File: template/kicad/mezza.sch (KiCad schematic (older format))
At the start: 2 parts, among them P1 CONN_02X20, P2 CONN_02X20

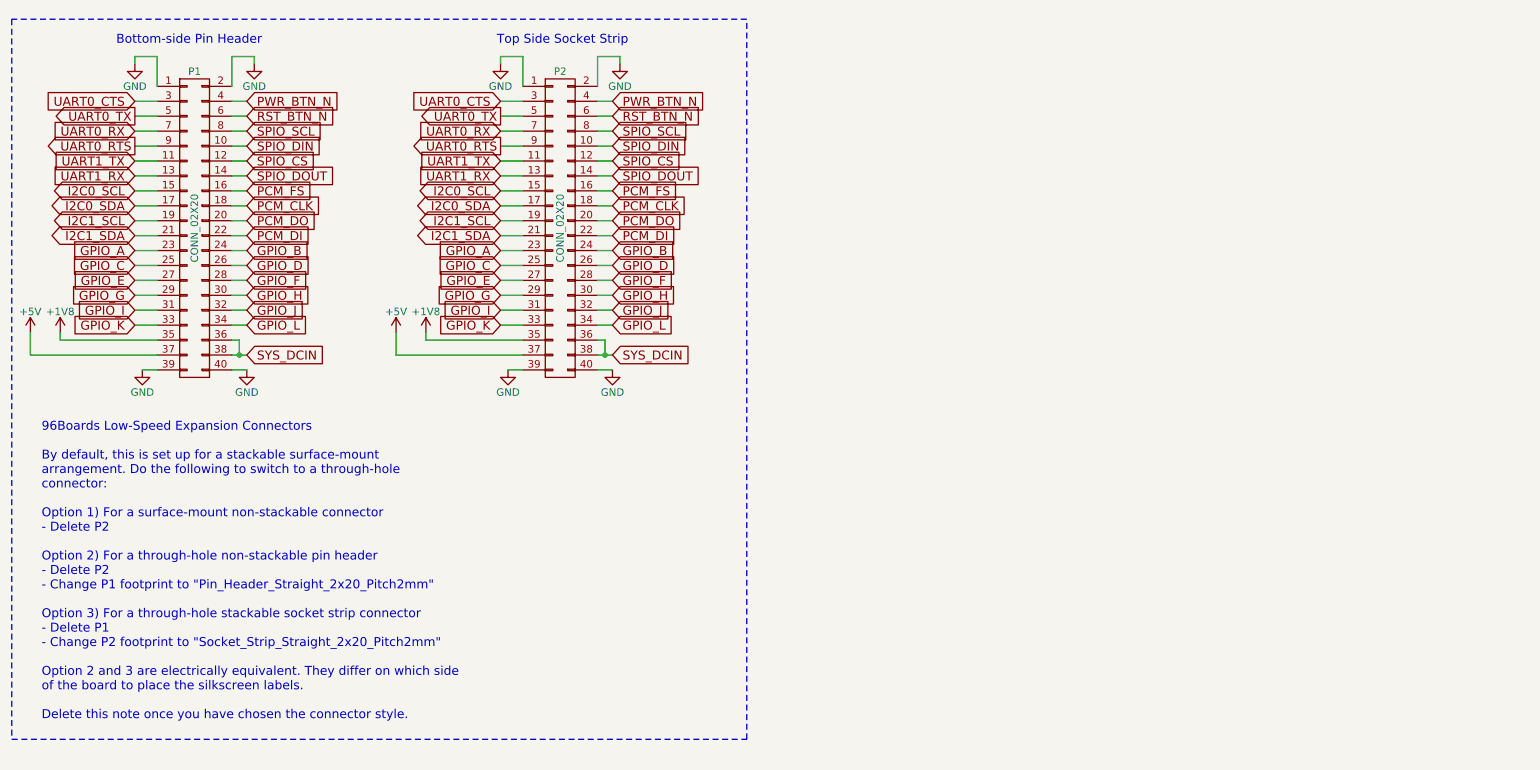
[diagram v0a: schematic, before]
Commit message: Add high speed connector to kicad template
Schematic connector added with net names.
3D model included for PCB footprint.

Signed-off-by: Michael Welling <mwelling@ieee.org>
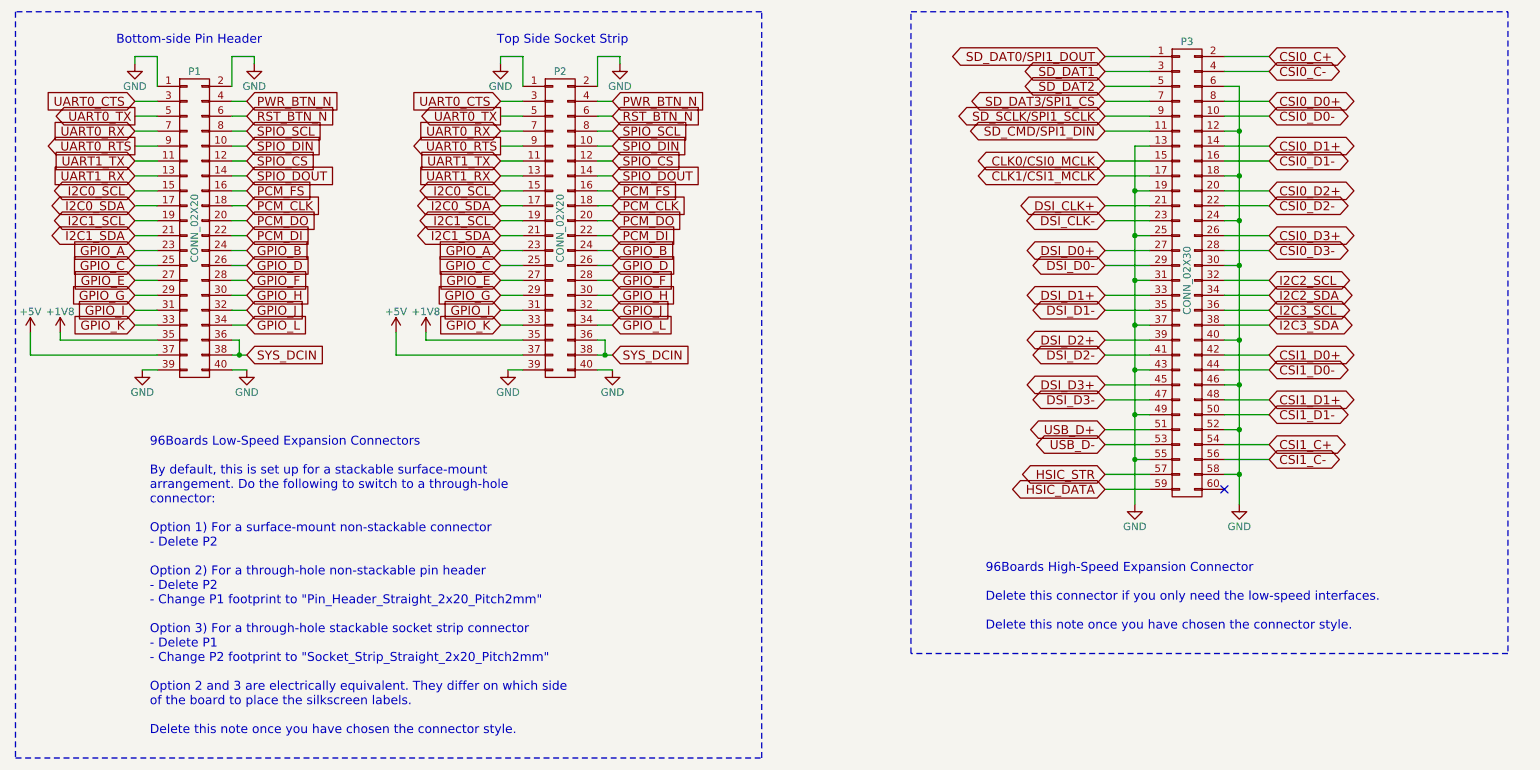
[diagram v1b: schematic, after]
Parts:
- added P3: CONN_02X30, 96boards:61083-063400LF, symbol CONN_02X30
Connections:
- net GND: now also P3.12 (P12), P3.13 (P13), P3.18 (P18), P3.19 (P19), P3.24 (P24), P3.25 (P25), P3.30 (P30), P3.31 (P31), P3.37 (P37), P3.40 (P40), P3.43 (P43), P3.46 (P46), P3.49 (P49), P3.52 (P52), P3.55 (P55), P3.58 (P58), P3.6 (P6)
- new net CLK0/CSI0_MCLK: P3.15 (P15)
- new net CLK1/CSI1_MCLK: P3.17 (P17)
- new net CSI0_C+: P3.2 (P2)
- new net CSI0_C-: P3.4 (P4)
- new net CSI0_D0+: P3.8 (P8)
- new net CSI0_D0-: P3.10 (P10)
- new net CSI0_D1+: P3.14 (P14)
- new net CSI0_D1-: P3.16 (P16)
- new net CSI0_D2+: P3.20 (P20)
- new net CSI0_D2-: P3.22 (P22)
- new net CSI0_D3+: P3.26 (P26)
- new net CSI0_D3-: P3.28 (P28)
- new net CSI1_C+: P3.54 (P54)
- new net CSI1_C-: P3.56 (P56)
- new net CSI1_D0+: P3.42 (P42)
- new net CSI1_D0-: P3.44 (P44)
- new net CSI1_D1+: P3.48 (P48)
- new net CSI1_D1-: P3.50 (P50)
- new net DSI_CLK+: P3.21 (P21)
- new net DSI_CLK-: P3.23 (P23)
- new net DSI_D0+: P3.27 (P27)
- new net DSI_D0-: P3.29 (P29)
- new net DSI_D1+: P3.33 (P33)
- new net DSI_D1-: P3.35 (P35)
- new net DSI_D2+: P3.39 (P39)
- new net DSI_D2-: P3.41 (P41)
- new net DSI_D3+: P3.45 (P45)
- new net DSI_D3-: P3.47 (P47)
- new net HSIC_DATA: P3.59 (P59)
- new net HSIC_STR: P3.57 (P57)
- new net I2C2_SCL: P3.32 (P32)
- new net I2C2_SDA: P3.34 (P34)
- new net I2C3_SCL: P3.36 (P36)
- new net I2C3_SDA: P3.38 (P38)
- new net SD_CMD/SPI1_DIN: P3.11 (P11)
- new net SD_DAT0/SPI1_DOUT: P3.1 (P1)
- new net SD_DAT1: P3.3 (P3)
- new net SD_DAT2: P3.5 (P5)
- new net SD_DAT3/SPI1_CS: P3.7 (P7)
- new net SD_SCLK/SPI1_SCLK: P3.9 (P9)
- new net USB_D+: P3.51 (P51)
- new net USB_D-: P3.53 (P53)
- no-connect marks 0 -> 1
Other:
- note added: "96Boards High-Speed Expansion Connector\n\nDelete this connector if you only need the low-speed interfaces.\n\nDelete this note once you have chosen the connector style."
